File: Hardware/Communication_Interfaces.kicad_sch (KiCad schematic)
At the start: 54 parts, among them Q2 2SD882, Q5 2SD882, Q6 2SD882, U1 TCAN3414DR, U10 LTV-356T, U11 LTV-356T, U12 LTV-356T, U14 LTV-356T, U3 MAX3485, U6 LTV-356T

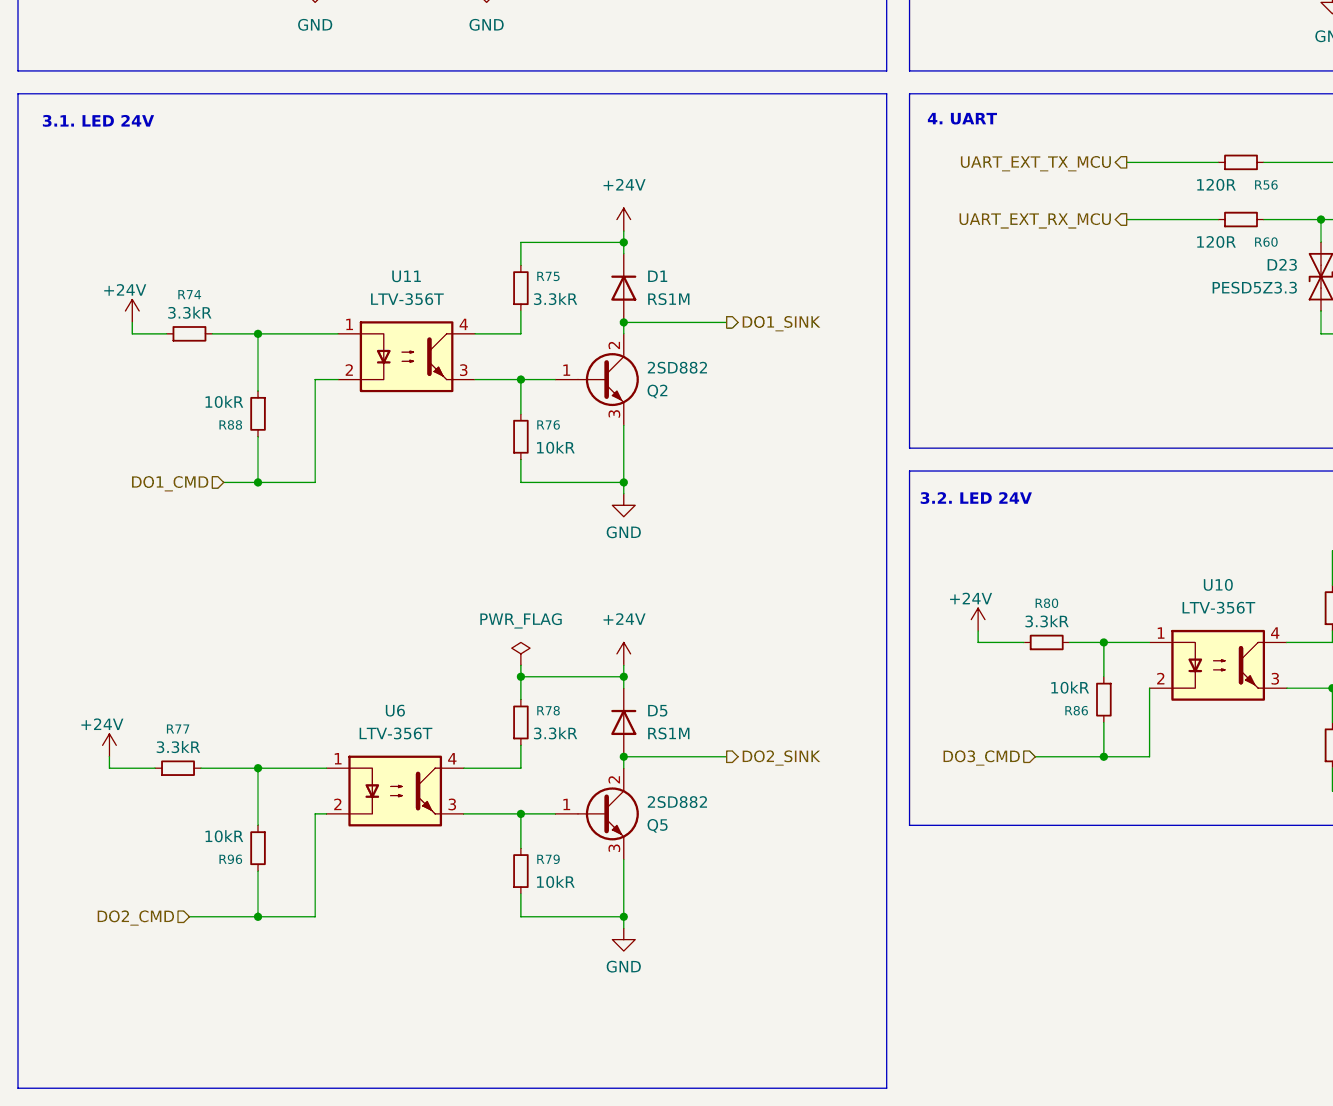
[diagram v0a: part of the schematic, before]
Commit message: fix(hardware): revise optocoupler control logic
Update relay and communication optocoupler drive networks, then synchronize the related PCB routing and KiCad project metadata.
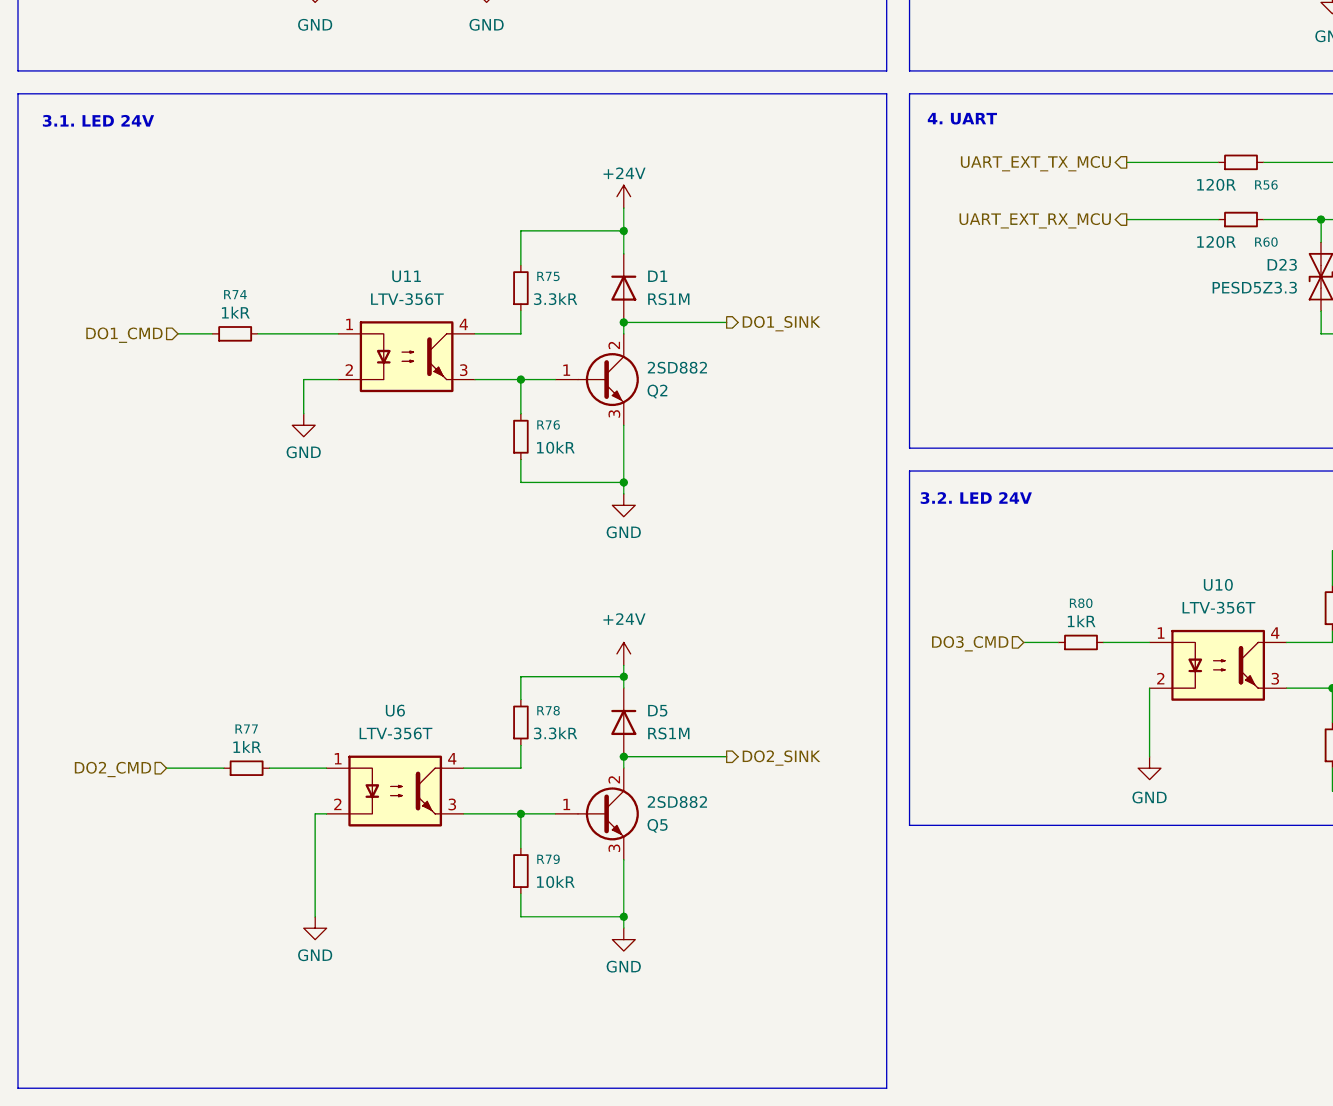
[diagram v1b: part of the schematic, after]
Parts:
- removed R86, R88, R96: 10kR, Resistor_SMD:R_0603_1608Metric, symbol Device:R_Small
- R74, R77, R80: value 3.3kR -> 1kR
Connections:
- net +24V: no longer R74.1, R77.1, R80.1
- net DO1_CMD: now also R74.1; no longer U11.2
- net DO2_CMD: now also R77.1; no longer U6.2
- net DO3_CMD: now also R80.1; no longer U10.2
- net GND: now also U10.2, U11.2, U6.2
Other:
- moved on the sheet: R74, R77, R80
